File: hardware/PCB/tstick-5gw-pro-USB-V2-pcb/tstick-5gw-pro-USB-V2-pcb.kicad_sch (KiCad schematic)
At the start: 57 parts, among them J1 USB_C_Receptacle_USB2.0, Q3 BSS138, SW1 JST-SH-1.00mm 1x2, SW2 PTS810 SJM Switch, SW3 PTS810 SJM Switch, U1 max8819ceti+, U4 PCA9306DP

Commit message: removed max8819 for cheaper pmic solution (mcp73871 + 2 regulators), updated BOM of esp32 board
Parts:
- removed L1, L2: 4.7uH, Inductor_SMD:L_0603_1608Metric, symbol Device:L
- removed R10, R8: 100k, Resistor_SMD:R_0201_0603Metric, symbol Device:R_US
- removed R11: 80.6k, Resistor_SMD:R_0201_0603Metric, symbol Device:R_US
- removed R9: 232k, Resistor_SMD:R_0201_0603Metric, symbol Device:R_US
- removed U1: max8819ceti+, max8819-footprints:21-0139_T2844&plus_1_MXM, symbol max8819-symbols:max8819ceti+
- removed U4: PCA9306DP, Package_SO:TSSOP-8_3x3mm_P0.65mm, symbol Interface:PCA9306DP
- added C11, C12: 1uF, Capacitor_SMD:C_0201_0603Metric, symbol Device:C
- added CHARGLED2, CHARGLED3: LED, LED_SMD:LED_0402_1005Metric, symbol Device:LED
- added D2: PESD5Z3.3,115, Diode_SMD:D_SOD-523, symbol Diode:ESD5Zxx
- added Q1, Q2: BSS138, Package_TO_SOT_SMD:SOT-23, symbol Transistor_FET:BSS138
- added R16: 2k2, Resistor_SMD:R_0201_0603Metric, symbol Device:R_US
- added R17: 24.9k, Resistor_SMD:R_0201_0603Metric, symbol Device:R_US
- added R22, R24: 1k, Resistor_SMD:R_0201_0603Metric, symbol Device:R_US
- added SYS3, SYS4, SYS5, SYS6: SYS, symbol power-symbols:VSYS
- added TH2: 10k, Resistor_SMD:R_0201_0603Metric, symbol Device:Thermistor_NTC_US
- added U2: MCP73871, Package_DFN_QFN:QFN-20-1EP_4x4mm_P0.5mm_EP2.5x2.5mm, symbol Battery_Management:MCP73871
- added U3: NCP167AMX330TBG, XDFN4_1X1_711AJ_ONS, symbol NCP167AMX330TBG:NCP167AMX330TBG
- added U4: NCP167AMX180TBG, XDFN4_1X1_711AJ_ONS, symbol NCP167:NCP167AMX180TBG
- C14: value 0.1uF -> 10uF; footprint Capacitor_SMD:C_0201_0603Metric -> Capacitor_SMD:C_0603_1608Metric; Description Value Pkg 0.1 µF ±10% 10V Ceramic Capacitor X5R 0201 (0603 Metric) -> 10 µF ±10% 6.3V Ceramic Capacitor X5R 0603 (1608 Metric); Digikey Part # 1276-1115-1-ND -> (none); Mfg Part # CL03A104KP3NNNC -> CL10A106KQ8NNNC
- C4, C5: value 22uF -> 1uF; footprint Capacitor_SMD:C_0603_1608Metric -> Capacitor_SMD:C_0201_0603Metric; Description Value Pkg 22 µF ±10% 6.3V Ceramic Capacitor X5R 0603 (1608 Metric) -> 1 µF ±10% 6.3V Ceramic Capacitor X5R 0201 (0603 Metric); Digikey Part # 1276-2867-1-ND -> 1276-1323-1-ND; Mfg Part # CL10A226KQ8NRNE -> CL03A105KQ3CSNC
- CHARGLED1: footprint LED_SMD:LED_0201_0603Metric -> LED_SMD:LED_0402_1005Metric; Description Value Pkg Green 525nm LED Indication - Discrete 2.85V 0201 (0603 Metr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 -> Red 630nm LED Indication - Discrete 1.95V 0402 (1005 Metric); Digikey Part # 754-APG0603ZGC-5MAVCT-ND -> (none); Mfg Part # APG0603ZGC-5MAV -> APHHS1005SURCK
- QWIIC1: Description Value Pkg Connector Header Surface Mount, Right Angle 4 position 0.03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 -> Connector Header Surface Mount 4 position 0.039" (1.00mm)
- R18: value 200k -> 330k; Description Value Pkg 200 kOhms ±1% 0.05W, 1/20W Chip Resistor 0201 (0603 Metric)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 -> 330 kOhms ±1% 0.05W, 1/20W Chip Resistor 0201 (0603 Metric)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; Digikey Part # P122814CT-ND -> (none); Mfg Part # ERJ-1GNF2003C -> ERJ-1GNF3303C
- R20: value 2k2 -> 2k; Description Value Pkg 2.2 kOhms ±1% 0.05W, 1/20W Chip Resistor 0201 (0603 Metric)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 -> RES SMD 2K OHM 1% 1/20W 0201; Digikey Part # P122832CT-ND -> (none); Mfg Part # ERJ-1GNF2201C -> ERJ-1GNF2001C
- R4: value 6.04k -> 110k; Description Value Pkg 6.04 kOhms ±1% 0.05W, 1/20W Chip Resistor 0201 (0603 Metric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 -> 110 kOhms ±1% 0.05W, 1/20W Chip Resistor 0201 (0603 Metric)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; Digikey Part # P123095CT-ND -> (none); Mfg Part # ERJ-1GNF6041C -> ERJ-1GNF1103C
- TrillExtensionInput1: value JST-SH 1x08 1.00mm -> JST-SH-1x04 1.0mm; Mfg Part # BM04B-SRSS-TB -> Connector Header Surface Mount 4 position 0.039" (1.00mm)
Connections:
- net +1V8: now also C12.1, Q1.1 (G), Q2.1 (G), U4.1 (OUT); no longer C5.1
- net +3V3: now also C5.1, R16.2, U3.1 (OUT); no longer C4.1, R18.2, R20.2
- net +BATT: now also U2.14 (V_{BAT}), U2.15 (V_{BAT}), U2.16 (V_{BAT_SENSE})
- net GND: now also R20.1, C11.2, C12.2, D2.2 (A), R17.1, TH2.1, U2.10 (V_{SS}), U2.11 (V_{SS}), U2.21 (V_{SS}), U2.3 (SEL), U2.9 (~{TE}), U3.2 (GND), U3.5 (GND), U4.2 (GND), U4.5 (GND)
- net LV_SCL: now also Q1.2 (S)
- net LV_SDA: now also Q2.2 (S)
- net SCL: now also Q1.3 (D)
- net SDA: now also Q2.3 (D), R16.1; no longer R20.1
- net STAT: now also U2.8 (STAT1/~{LBO})
- net SYS: now also C4.1, C11.1, SYS3.1 (SYS), SYS4.1 (SYS), SYS5.1 (SYS), SYS6.1 (SYS), U2.1 (OUT), U2.17 (CE), U2.20 (OUT), U2.4 (PROG2), U3.3 (EN), U3.4 (IN), U4.3 (EN), U4.4 (IN); no longer CHARGLED1.2 (A)
- net VUSB: now also C14.1, CHARGLED1.2 (A), R18.2, CHARGLED2.2 (A), CHARGLED3.2 (A), D2.1 (K), U2.18 (IN), U2.19 (IN)
- net ISET renamed VPCC
- net VPCC: now also R18.1, U2.2 (VPCC)
- removed net LS_EN: C14.1, R18.1
- new net: CHARGLED2.1 (K), R22.1
- new net: CHARGLED3.1 (K), R24.1
- new net PG: R24.2, U2.6 (~{PG})
- new net PROG1: R20.2, U2.13 (PROG1)
- new net PROG3: R17.2, U2.12 (PROG3)
- new net STAT2: R22.2, U2.7 (STAT2)
- new net THERM: TH2.2, U2.5 (THERM)
- no-connect marks 8 -> 6
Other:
- note added: "Bypass Capacitor"
- note added: "Charge Limit 2kOhm = 500mA"
- note added: "Charge Termincation Current 24.9koHm = 40mA charge termination"
- note added: "Comms - SDA: IO12 - SCL: IO11 - USBD+: IO20 - USBD-: IO19 Peripherals - FSR: IO9 - Button: IO3 - UART TX: IO43 - UART RX: IO44 - Status LED: IO46 Interrupts - IMU Interrupt: IO21 - Fuel Gauge Interrupt: IO17 - Touch Interrupt 1: IO42 - Touch Interrupt 2: IO41 - Touch Interrupt 3: IO40 - Touch Interrupt 4: IO39"
- note added: "Voltage Charge Control"
- note removed: "Charge Limit 6.04kOhm = 497mA"
- note removed: "Comms - SDA: IO12 - SCL: IO11 - USBD+: IO20 - USBD-: IO19 Peripherals - FSR: IO9 - Button: IO3 - UART TX: IO43 - UART RX: IO44 - Status LED: IO46 Interrupts - IMU Interrupt: IO21 - Fuel Gauge Interrupt: IO17 - Touch Interrupt 1: IO39 - Touch Interrupt 2: IO40 - Touch Interrupt 3: IO41 - Touch Interrupt 4: IO42"
- note removed: "Resistor values give 3.32V output"
- note removed: "SYS is the System Voltage, set to 4.35V by main regulator"
- moved on the sheet: C13, C3, PWLED1, R13, R14, R19

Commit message: added updated bill of materials and manufacturing files
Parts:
- removed D2: PESD5Z3.3,115, Diode_SMD:D_SOD-523, symbol Diode:ESD5Zxx
- removed SYS2, SYS4: SYS, symbol power-symbols:VSYS
- added C15: 0.1uF, Capacitor_SMD:C_0201_0603Metric, symbol Device:C
- added U1: USBLC6-2P6, Package_TO_SOT_SMD:SOT-666, symbol Power_Protection:USBLC6-2P6
- R20: Description Value Pkg RES SMD 2K OHM 1% 1/20W 0201 -> 2 kOhms ±1% 0.05W, 1/20W Chip Resistor 0201 (0603 Metric) T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
- U3: Description Value Pkg Linear Voltage Regulator IC Positive Fixed 1 Output 700mA 4-XDFN (1x1) -> Linear Voltage Regulator IC Positive Fixed 1 Output 700mA 4-XDFN (1x1), 3.3V
- U4: Description Value Pkg Linear Voltage Regulator IC Positive Fixed 1 Output 700mA 4-XDFN (1x1) -> Linear Voltage Regulator IC Positive Fixed 1 Output 700mA 4-XDFN (1x1), 1.8V
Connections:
- net GND: now also C15.2, U1.2 (GND); no longer U2.3 (SEL)
- net SYS: no longer U2.17 (CE), U2.4 (PROG2)
- net USBD+: now also U1.4 (I/O2); no longer J1.A6 (D+), J1.B6 (D+)
- net USBD-: now also U1.6 (I/O1); no longer J1.A7 (D-), J1.B7 (D-)
- net VUSB: now also U2.17 (CE), U2.3 (SEL), U2.4 (PROG2), C15.1, U1.5 (VBUS)
- new net D+: J1.A6 (D+), J1.B6 (D+), U1.3 (I/O2)
- new net D-: J1.A7 (D-), J1.B7 (D-), U1.1 (I/O1)
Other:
- moved on the sheet: QWIIC1, R22, R24, R3

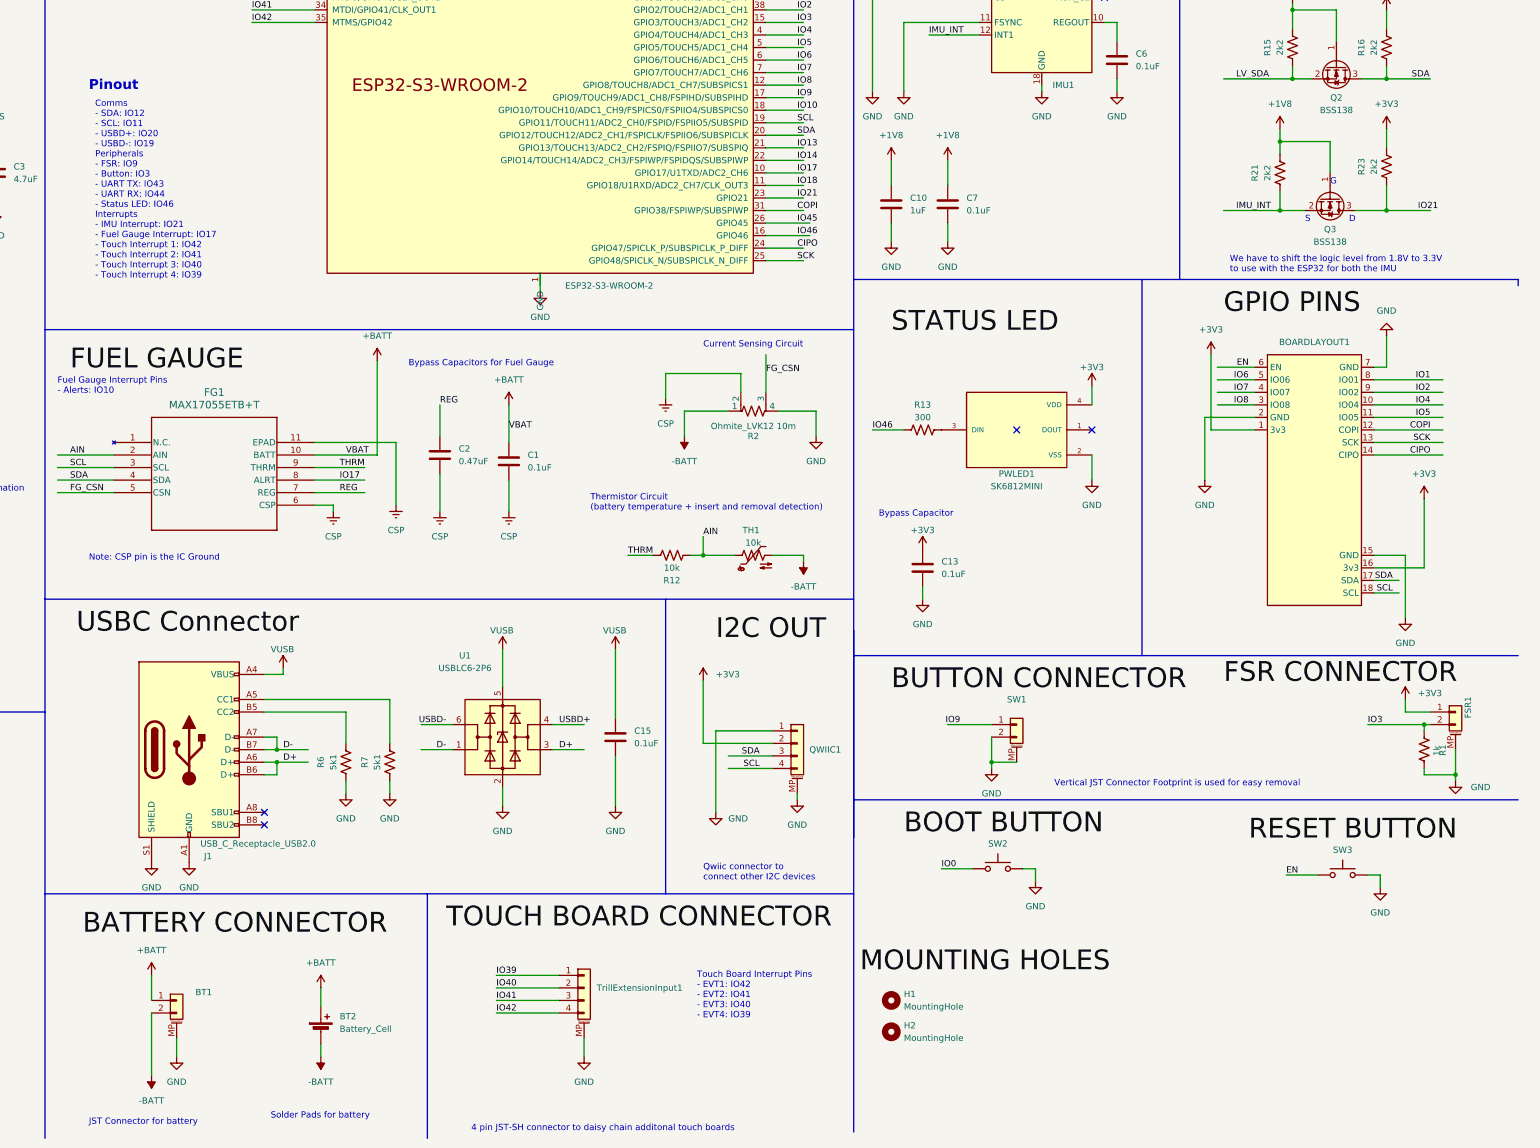
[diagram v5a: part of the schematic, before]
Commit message: reduced size of esp32 pcb to 1x2.35 inch, used ssmaller neopixel, updated BOM
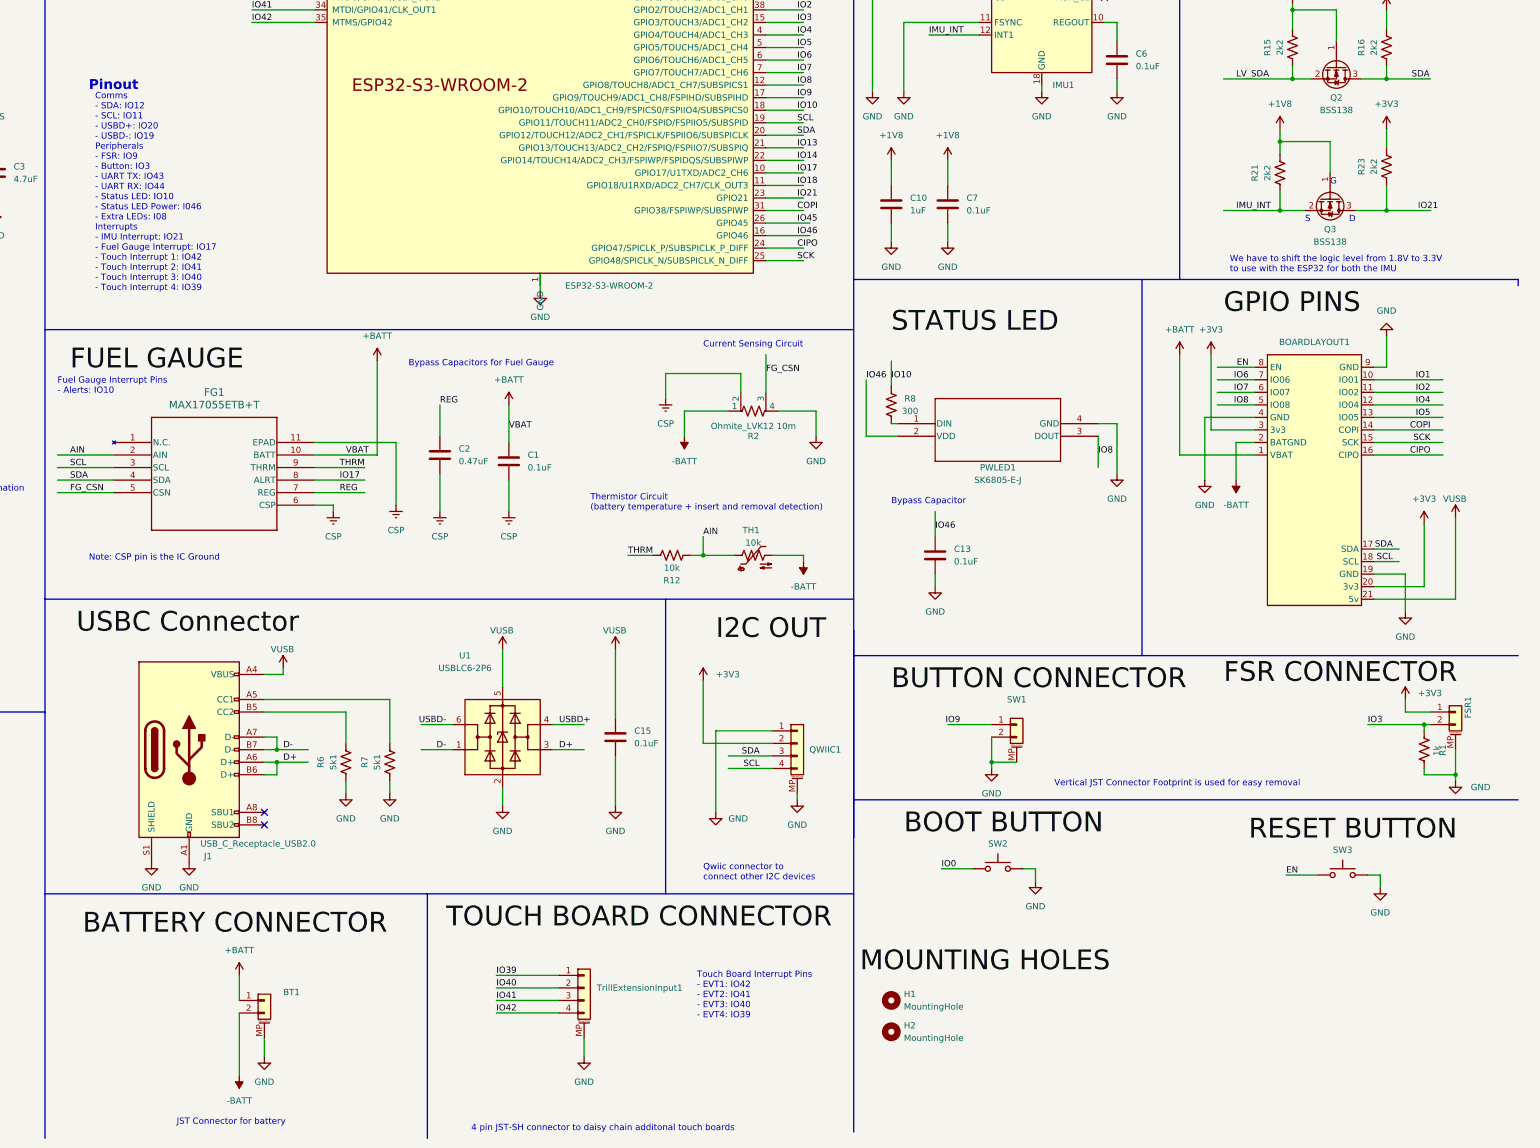
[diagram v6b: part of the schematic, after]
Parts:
- removed BT2: Battery_Cell, solderpads:SolderPad, symbol Device:Battery_Cell
- removed R13: 300, Resistor_SMD:R_0201_0603Metric, symbol Device:R_US
- added R8: 300, Resistor_SMD:R_0201_0603Metric, symbol Device:R_US
- PWLED1: value SK6812MINI -> SK6805-E-J; footprint neopixel:2659 -> neopixel-1515-footprints:4492_ADA; symbol neopixel:2659 -> neopixel-1515:4492; Description Value Pkg Addressable Lighting Neopixel 10 LED Discrete Serial (Shift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 -> Addressable Lighting Neopixel 10 LED Discrete Red, Green, B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; Digikey Part # 1528-1542-ND -> 1528-4492-ND; Mfg Part # 2659 -> 4492
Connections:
- net +3V3: now also BOARDLAYOUT1.20 (3v3), BOARDLAYOUT1.3 (3v3); no longer BOARDLAYOUT1.1 (3v3), BOARDLAYOUT1.16 (3v3), C13.1, PWLED1.4 (VDD)
- net +BATT: now also BOARDLAYOUT1.1 (VBAT)
- net -BATT: now also BOARDLAYOUT1.2 (BATGND)
- net CIPO: now also BOARDLAYOUT1.16 (CIPO); no longer BOARDLAYOUT1.14 (CIPO)
- net COPI: now also BOARDLAYOUT1.14 (COPI); no longer BOARDLAYOUT1.12 (COPI)
- net EN: now also BOARDLAYOUT1.8 (EN); no longer BOARDLAYOUT1.6 (EN)
- net GND: now also BOARDLAYOUT1.19 (GND), BOARDLAYOUT1.4 (GND), BOARDLAYOUT1.9 (GND), PWLED1.4 (GND); no longer BOARDLAYOUT1.15 (GND), BOARDLAYOUT1.2 (GND), BOARDLAYOUT1.7 (GND), PWLED1.2 (VSS)
- net IO1: now also BOARDLAYOUT1.10 (IO01); no longer BOARDLAYOUT1.8 (IO01)
- net IO10: now also R8.1
- net IO2: now also BOARDLAYOUT1.11 (IO02); no longer BOARDLAYOUT1.9 (IO02)
- net IO4: now also BOARDLAYOUT1.12 (IO04); no longer BOARDLAYOUT1.10 (IO04)
- net IO46: now also C13.1, PWLED1.2 (VDD)
- net IO5: now also BOARDLAYOUT1.13 (IO05); no longer BOARDLAYOUT1.11 (IO05)
- net IO6: now also BOARDLAYOUT1.7 (IO06); no longer BOARDLAYOUT1.5 (IO06)
- net IO7: now also BOARDLAYOUT1.6 (IO07); no longer BOARDLAYOUT1.4 (IO07)
- net IO8: now also BOARDLAYOUT1.5 (IO08), PWLED1.3 (DOUT); no longer BOARDLAYOUT1.3 (IO08)
- net SCK: now also BOARDLAYOUT1.15 (SCK); no longer BOARDLAYOUT1.13 (SCK)
- net VUSB: now also BOARDLAYOUT1.21 (5v)
- net at PWLED1.1 (DIN): now also R8.2
- no-connect marks 6 -> 4
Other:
- note added: "Comms - SDA: IO12 - SCL: IO11 - USBD+: IO20 - USBD-: IO19 Peripherals - FSR: IO9 - Button: IO3 - UART TX: IO43 - UART RX: IO44 - Status LED: IO10 - Status LED Power: I046 - Extra LEDs: I08 Interrupts - IMU Interrupt: IO21 - Fuel Gauge Interrupt: IO17 - Touch Interrupt 1: IO42 - Touch Interrupt 2: IO41 - Touch Interrupt 3: IO40 - Touch Interrupt 4: IO39"
- note removed: "Comms - SDA: IO12 - SCL: IO11 - USBD+: IO20 - USBD-: IO19 Peripherals - FSR: IO9 - Button: IO3 - UART TX: IO43 - UART RX: IO44 - Status LED: IO46 Interrupts - IMU Interrupt: IO21 - Fuel Gauge Interrupt: IO17 - Touch Interrupt 1: IO42 - Touch Interrupt 2: IO41 - Touch Interrupt 3: IO40 - Touch Interrupt 4: IO39"
- note removed: "Solder Pads for battery"
- moved on the sheet: BT1
